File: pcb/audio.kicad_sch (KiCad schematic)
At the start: 76 parts, among them J9 Headphones, Q10 BC547, Q11 BC338, Q12 BC328, Q7 BC547, Q8 BC547, Q9 BC547, U58 74HC245, U59 4504, U60 4053, U61 4053, U62 4504, U63 4053, U64 TL072, U65 4053, U66 TL074, U67 LM7809_TO220, U68 LM7805_TO220, U69 LM7909_TO220

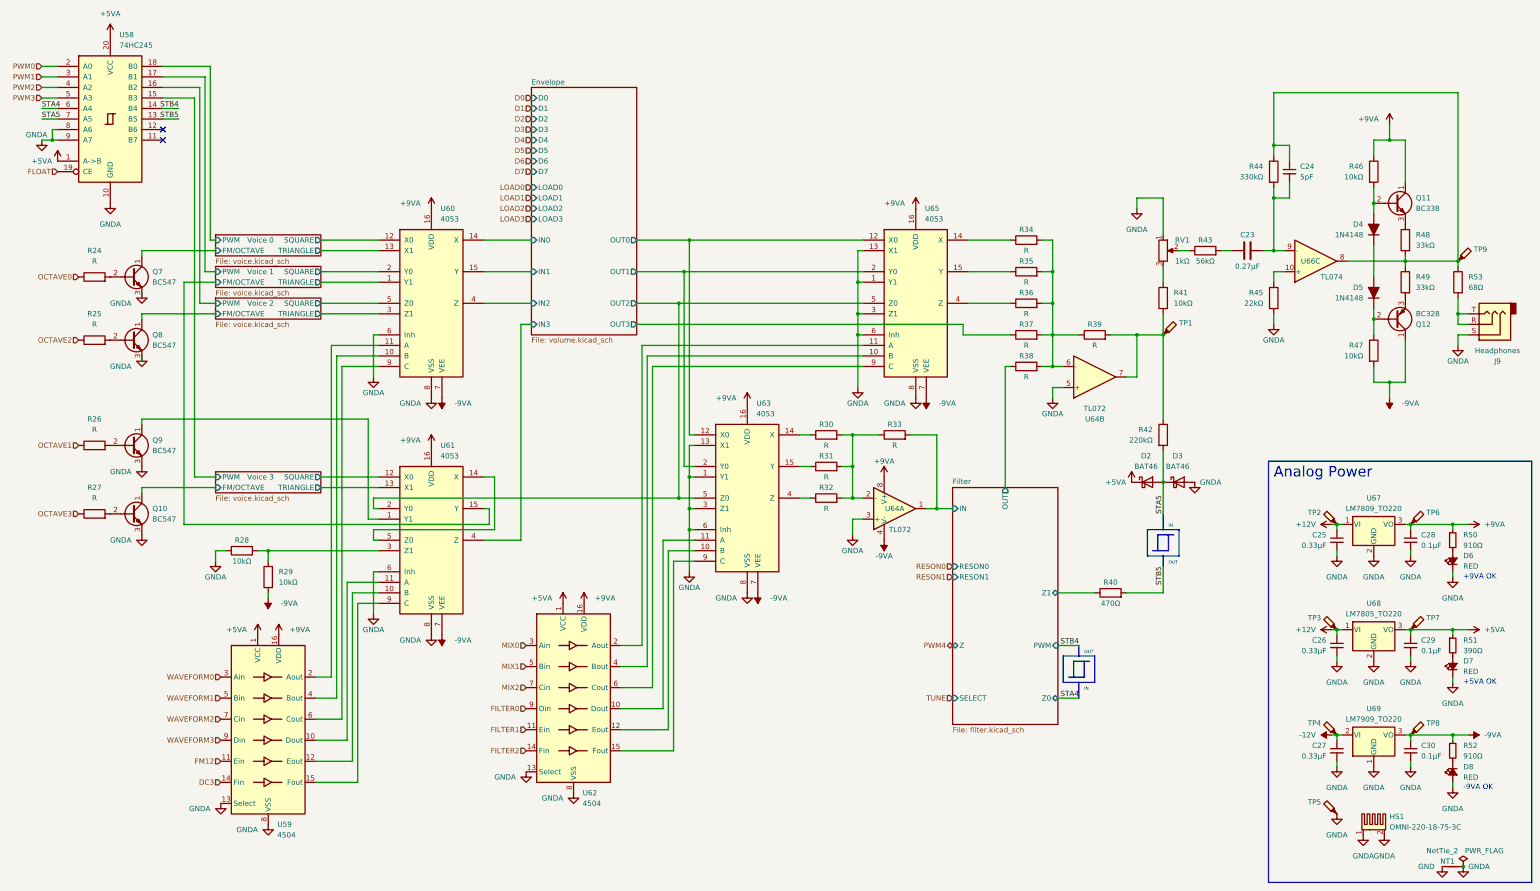
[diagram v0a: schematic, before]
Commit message: WIP PCB (add bypass caps, minor fixes)
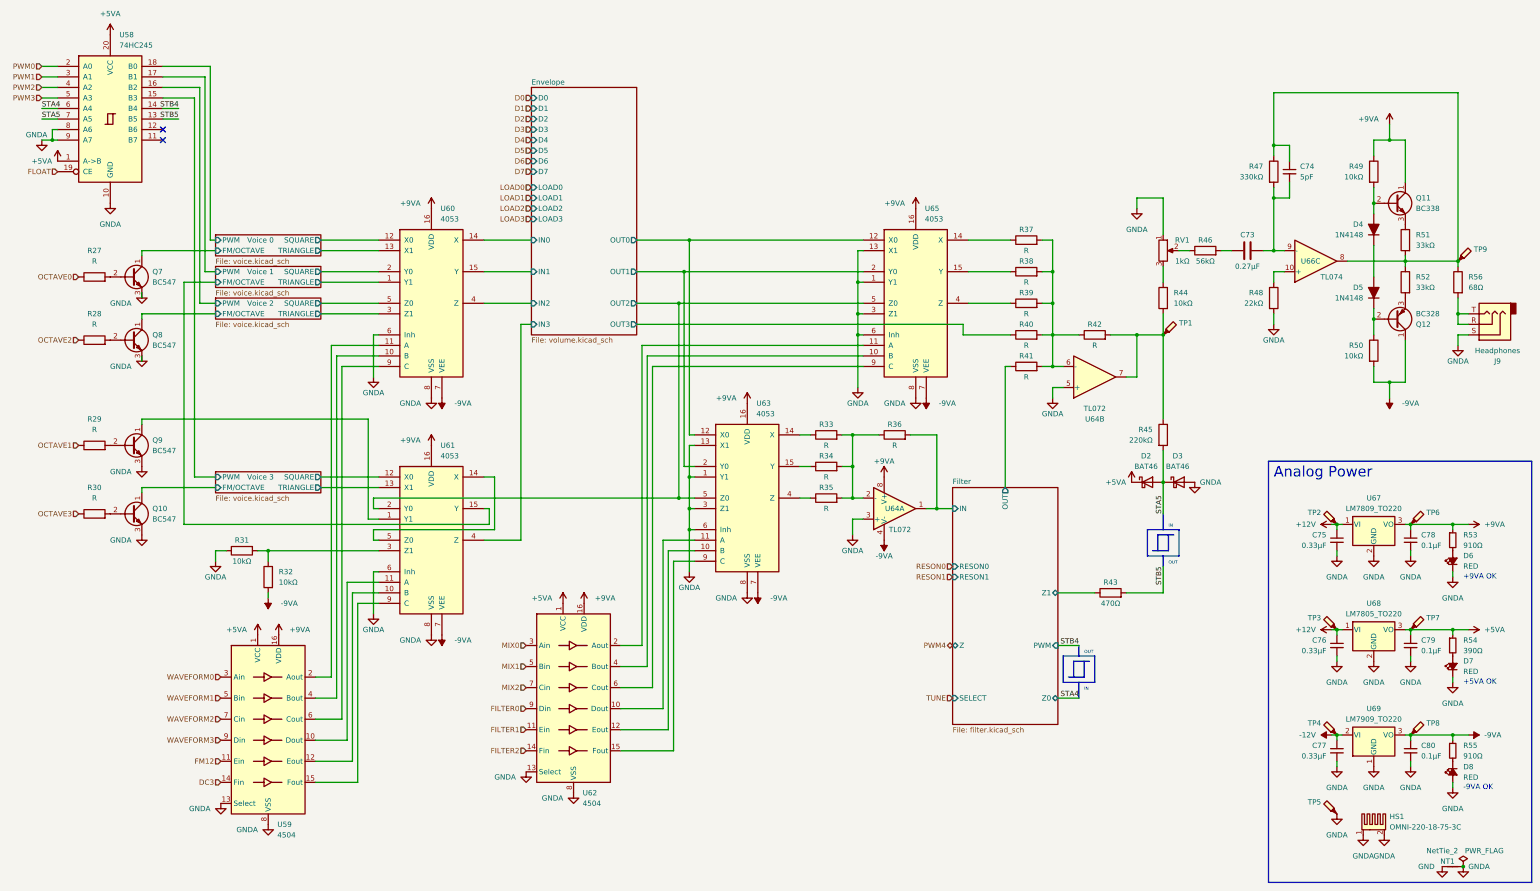
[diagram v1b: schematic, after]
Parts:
- renumbered C23 to C73, C24 to C74, C25 to C75, C26 to C76, C27 to C77, C28 to C78, C29 to C79, C30 to C80, R24 to R27, R25 to R28, R26 to R29, R27 to R30, R28 to R31, R29 to R32, R30 to R33, R31 to R34, R32 to R35, R33 to R36, R34 to R37, R35 to R38, R36 to R39, R37 to R40, R38 to R41, R39 to R42, R40 to R43, R41 to R44, R42 to R45, R43 to R46, R44 to R47, R45 to R48, R46 to R49, R47 to R50, R48 to R51, R49 to R52, R50 to R53, R51 to R54, R52 to R55, R53 to R56
